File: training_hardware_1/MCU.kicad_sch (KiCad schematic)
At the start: 2 parts, among them J1 RJ45_LED_Shielded, U1 Teensy4.1_DEV-16771

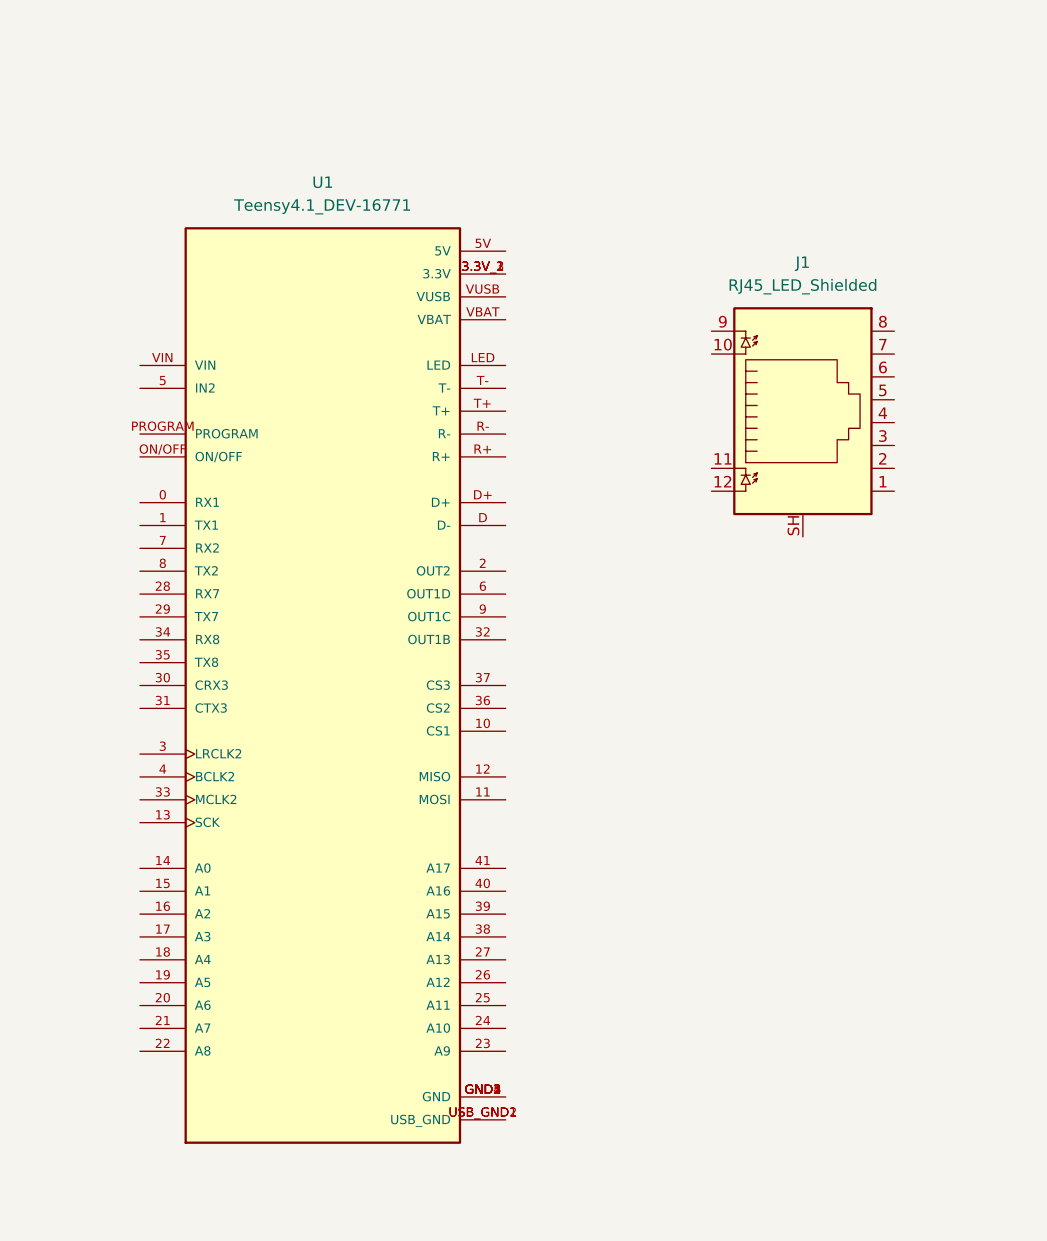
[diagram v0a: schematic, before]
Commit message: Add Ethernet
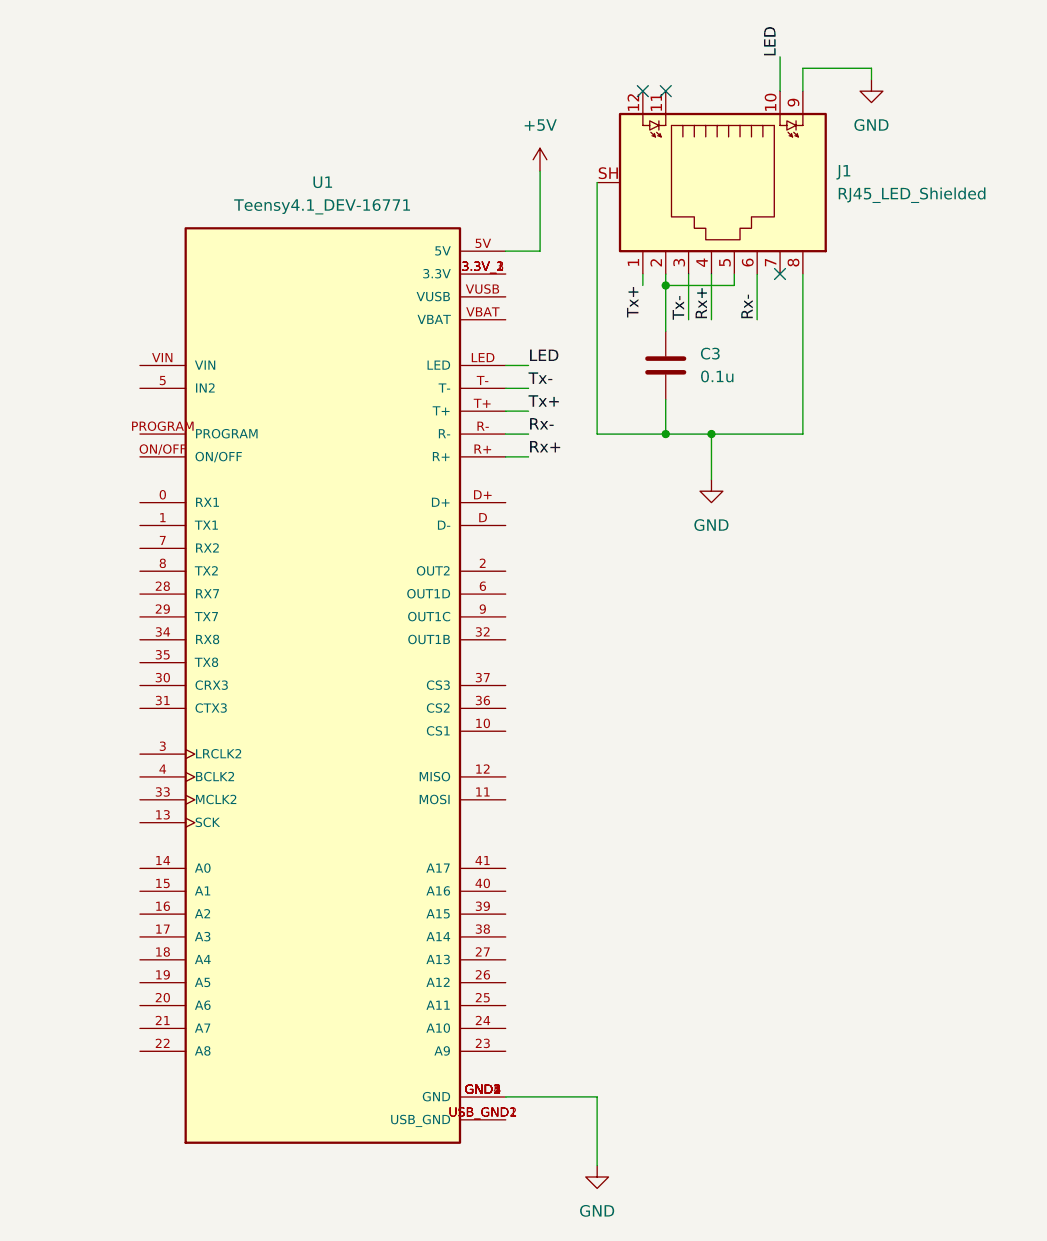
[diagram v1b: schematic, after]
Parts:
- added C3: 0.1u, symbol Device:C
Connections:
- net +5V: now reaches U1.5V
- net GND: now reaches U1.GND1 (GND), U1.GND2 (GND), U1.GND3 (GND), U1.GND4 (GND), U1.GND5 (GND)
- net GND: now also J1.8, J1.9, J1.SH, C3.2
- net LED: now reaches U1.LED
- net LED: now also J1.10
- net Rx+: now reaches U1.R+
- net Rx+: now also J1.4
- net Rx-: now reaches U1.R-
- net Rx-: now also J1.6
- net Tx+: now reaches U1.T+
- net Tx+: now also J1.1
- net Tx-: now reaches U1.T-
- net Tx-: now also J1.3
- net at J1.2: now also J1.5, C3.1
- no-connect marks 0 -> 3
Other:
- moved on the sheet: J1

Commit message: Finish Schematic
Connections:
- net STBY: now reaches U1.2 (OUT2)
- net CTX1: now reaches U1.22 (A8)
- net CRX1: now reaches U1.23 (A9)
- net +3V3: now reaches U1.3.3V_1 (3.3V), U1.3.3V_2 (3.3V), U1.3.3V_3 (3.3V)
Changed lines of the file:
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@@
+	(wire
+		(pts
+			(xy 196.85 52.07) (xy 204.47 52.07)
+		)
+		(stroke
+			(width 0)
+			(type default)
+		)
+	)
+	(wire
+		(pts
+			(xy 196.85 85.09) (xy 203.2 85.09)
+		)
+		(stroke
+			(width 0)
+			(type default)
+		)
+	)
 	(wire
 		(pts
@@
 	(wire
 		(pts
+			(xy 149.86 138.43) (xy 156.21 138.43)
+		)
+		(stroke
+			(width 0)
+			(type default)
+		)
+	)
+	(wire
+		(pts
 			(xy 200.66 40.64) (xy 200.66 49.53)
 		)
@@
 	(wire
 		(pts
+			(xy 204.47 33.02) (xy 204.47 52.07)
+		)
+		(stroke
+			(width 0)
+			(type default)
+		)
+	)
+	(wire
+		(pts
 			(xy 219.71 74.93) (xy 219.71 69.85)
 		)
@@
 		(pts
 			(xy 214.63 69.85) (xy 219.71 69.85)
+		)
+		(stroke
+			(width 0)
+			(type default)
+		)
+	)
+	(wire
+		(pts
+			(xy 196.85 138.43) (xy 205.74 138.43)
 		)
 		(stroke
@@
 			)
 			(justify left bottom)
+		)
+	)
+	(hierarchical_label "CTX1"
+		(shape input)
+		(at 149.86 138.43 180)
+		(effects
+			(font
+				(size 1.27 1.27)
+			)
+			(justify right)
+		)
+	)
+	(hierarchical_label "CRX1"
+		(shape input)
+		(at 205.74 138.43 0)
+		(effects
+			(font
+				(size 1.27 1.27)
+			)
+			(justify left)
+		)
+	)
+	(hierarchical_label "STBY"
+		(shape output)
+		(at 203.2 85.09 0)
+		(effects
+			(font
+				(size 1.27 1.27)
+			)
+			(justify left)
 		)
 	)
@@
 					(unit 1)
 				)
+			)
+		)
+	)
+	(symbol
+		(lib_id "power:+3V3")
+		(at 204.47 33.02 0)
+		(unit 1)
+		(exclude_from_sim no)
+		(in_bom yes)
+		(on_board yes)
+		(dnp no)
+		(fields_autoplaced yes)
+		(property "Reference" "#PWR016"
+			(at 204.47 36.83 0)
+			(effects
+				(font
+					(size 1.27 1.27)
+				)
+				(hide yes)
+			)
+		)
+		(property "Value" "+3V3"
+			(at 204.47 27.94 0)
+			(effects
+				(font
+					(size 1.27 1.27)
+				)
+			)
+		)
+		(property "Footprint" ""
+			(at 204.47 33.02 0)
+			(effects
+				(font
+					(size 1.27 1.27)
+				)
+				(hide yes)
+			)
+		)
+		(property "Datasheet" ""
+			(at 204.47 33.02 0)
+			(effects
+				(font
+					(size 1.27 1.27)
+				)
+				(hide yes)
+			)
+		)
+		(property "Description" "Power symbol creates a global label with name \"+3V3\""
+			(at 204.47 33.02 0)
+			(effects
+				(font
+					(size 1.27 1.27)
+				)
+				(hide yes)
+			)
+		)
+		(pin "1"
+		)
+		(instances
+			(project ""
+				(path "/7ad66101-d49b-4767-9ce8-b98c98937367/f8e32be3-5f9f-413c-af9c-31119b50f242"
+					(reference "#PWR016")
+					(unit 1)
+				)

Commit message: 11:34 in
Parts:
- C3: footprint (none) -> Capacitor_SMD:C_0603_1608Metric_Pad1.08x0.95mm_HandSolder
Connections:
- no-connect marks 3 -> 50
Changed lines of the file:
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@@
+	)
+	(no_connect
+		(at 156.21 77.47)
+	)
+	(no_connect
+		(at 156.21 105.41)
+	)
+	(no_connect
+		(at 156.21 80.01)
+	)
+	(no_connect
+		(at 156.21 125.73)
+	)
+	(no_connect
+		(at 196.85 128.27)
+	)
+	(no_connect
+		(at 196.85 123.19)
+	)
+	(no_connect
+		(at 196.85 87.63)
+	)
+	(no_connect
+		(at 196.85 92.71)
+	)
+	(no_connect
+		(at 196.85 80.01)
+	)
+	(no_connect
+		(at 196.85 102.87)
+	)
+	(no_connect
+		(at 156.21 118.11)
+	)
+	(no_connect
+		(at 156.21 87.63)
+	)
+	(no_connect
+		(at 196.85 120.65)
+	)
+	(no_connect
+		(at 156.21 69.85)
+	)
+	(no_connect
+		(at 196.85 133.35)
+	)
+	(no_connect
+		(at 196.85 54.61)
+	)
+	(no_connect
+		(at 156.21 100.33)
+	)
+	(no_connect
+		(at 156.21 82.55)
+	)
+	(no_connect
+		(at 156.21 62.23)
+	)
+	(no_connect
+		(at 156.21 110.49)
+	)
+	(no_connect
+		(at 156.21 128.27)
 	)
 	(no_connect
@@
 	)
 	(no_connect
+		(at 196.85 97.79)
+	)
+	(no_connect
+		(at 156.21 123.19)
+	)
+	(no_connect
+		(at 196.85 130.81)
+	)
+	(no_connect
+		(at 156.21 64.77)
+	)
+	(no_connect
+		(at 156.21 90.17)
+	)
+	(no_connect
+		(at 156.21 97.79)
+	)
+	(no_connect
+		(at 196.85 77.47)
+	)
+	(no_connect
+		(at 156.21 107.95)
+	)
+	(no_connect
+		(at 196.85 90.17)
+	)
+	(no_connect
+		(at 196.85 107.95)
+	)
+	(no_connect
+		(at 156.21 85.09)
+	)
+	(no_connect
 		(at 227.33 52.07)
 	)
 	(no_connect
+		(at 156.21 130.81)
+	)
+	(no_connect
+		(at 156.21 113.03)
+	)
+	(no_connect
+		(at 156.21 92.71)
+	)
+	(no_connect
+		(at 196.85 100.33)
+	)
+	(no_connect
+		(at 156.21 133.35)
+	)
+	(no_connect
+		(at 156.21 120.65)
+	)
+	(no_connect
+		(at 156.21 72.39)
+	)
+	(no_connect
+		(at 156.21 95.25)
+	)
+	(no_connect
+		(at 196.85 110.49)
+	)
+	(no_connect
 		(at 214.63 31.75)
+	)
+	(no_connect
+		(at 196.85 57.15)
+	)
+	(no_connect
+		(at 196.85 125.73)
+	)
+	(no_connect
+		(at 196.85 118.11)
+	)
+	(no_connect
+		(at 196.85 146.05)
+	)
+	(no_connect
+		(at 196.85 135.89)
+	)
+	(no_connect
+		(at 156.21 135.89)
 	)
 	(wire
@@
 			)
 		)
-		(property "Footprint" ""
+		(property "Footprint" "Capacitor_SMD:C_0603_1608Metric_Pad1.08x0.95mm_HandSolder"
 			(at 215.5952 66.04 0)
 			(effects

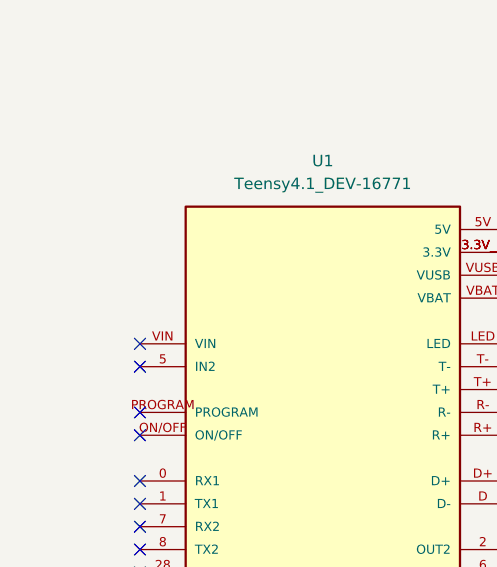
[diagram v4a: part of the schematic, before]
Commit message: Add components and wires(1:28)
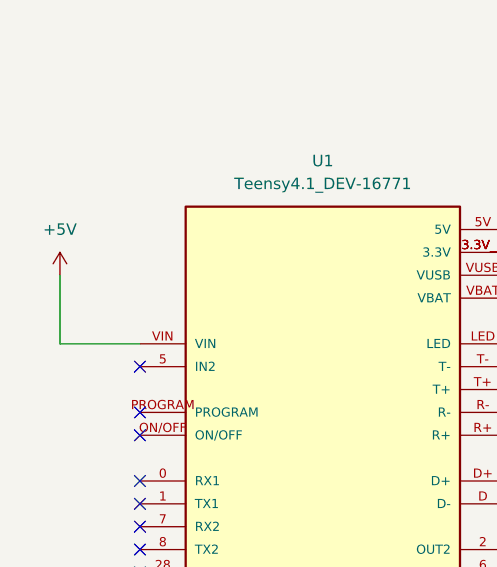
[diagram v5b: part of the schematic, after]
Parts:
- J1: footprint (none) -> MRDT_Connectors:RJ45_Teensy
- U1: footprint MODULE_DEV-16771 -> MRDT_Shields:Teensy_4_1_Ethernet
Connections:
- net +5V: now also U1.VIN
- no-connect marks 50 -> 49
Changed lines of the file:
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@@
-	)
-	(no_connect
-		(at 156.21 62.23)
 	)
 	(no_connect
@@
 	(wire
 		(pts
+			(xy 147.32 54.61) (xy 147.32 62.23)
+		)
+		(stroke
+			(width 0)
+			(type default)
+		)
+	)
+	(wire
+		(pts
 			(xy 229.87 29.21) (xy 237.49 29.21)
+		)
+		(stroke
+			(width 0)
+			(type default)
+		)
+	)
+	(wire
+		(pts
+			(xy 147.32 62.23) (xy 156.21 62.23)
 		)
 		(stroke
@@
 			)
 		)
-		(property "Footprint" "MODULE_DEV-16771"
+		(property "Footprint" "MRDT_Shields:Teensy_4_1_Ethernet"
 			(at 229.87 105.41 0)
 			(effects
@@
 	)
 	(symbol
+		(lib_id "power:+5V")
+		(at 147.32 54.61 0)
+		(unit 1)
+		(exclude_from_sim no)
+		(in_bom yes)
+		(on_board yes)
+		(dnp no)
+		(fields_autoplaced yes)
+		(property "Reference" "#PWR017"
+			(at 147.32 58.42 0)
+			(effects
+				(font
+					(size 1.27 1.27)
+				)
+				(hide yes)
+			)
+		)
+		(property "Value" "+5V"
+			(at 147.32 49.53 0)
+			(effects
+				(font
+					(size 1.27 1.27)
+				)
+			)
+		)
+		(property "Footprint" ""
+			(at 147.32 54.61 0)
+			(effects
+				(font
+					(size 1.27 1.27)
+				)
+				(hide yes)
+			)
+		)
+		(property "Datasheet" ""
+			(at 147.32 54.61 0)
+			(effects
+				(font
+					(size 1.27 1.27)
+				)
+				(hide yes)
+			)
+		)
+		(property "Description" "Power symbol creates a global label with name \"+5V\""
+			(at 147.32 54.61 0)
+			(effects
+				(font
+					(size 1.27 1.27)
+				)
+				(hide yes)
+			)
+		)
+		(pin "1"
+		)
+		(instances
+			(project "training_hardware_1"
+				(path "/7ad66101-d49b-4767-9ce8-b98c98937367/f8e32be3-5f9f-413c-af9c-31119b50f242"
+					(reference "#PWR017")
+					(unit 1)
+				)
+			)
+		)
+	)
+	(symbol
 		(lib_id "power:GND")
 		(at 219.71 74.93 0)
@@
 			)
 		)
-		(property "Footprint" ""
+		(property "Footprint" "MRDT_Connectors:RJ45_Teensy"
 			(at 220.345 41.91 90)
 			(effects
